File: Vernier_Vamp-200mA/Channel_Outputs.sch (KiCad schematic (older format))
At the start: 63 parts, among them U12 OPA2277, U13 OPA2277, U14 OPA2277, U15 OPA1622, U16 OPA1622, U17 OPA1622

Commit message: Coil driver version 1.0B
Updated coil driver 200mA version with fixes requested by Iain.
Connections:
- net labels added: +7.5V, -7.5V
- net labels removed: +8V, -8V
- wire segments 240 -> 239
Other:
- note added: "OP-AMP decoupling"
- moved on the sheet: C1, C2, C3, C31, C32, C33, C37, C38, C39, C40, C41, C42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

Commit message: OPA1622 Power Pad Tented Vias
-Created a footprint for OPA1622 that features tented vias on the power pad

-Applied it to the schematic as well as layout
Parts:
- U15, U16, U17: footprint Package_SON:Texas_S-PVSON-N10_ThermalVias -> PVSON-10_ThermalVias-Tented:Texas_S-PVSON-10_ThermalVias-Tented
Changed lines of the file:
@@
 $Descr A4 11693 8268
 encoding utf-8
-Sheet 7 7
+Sheet 6 7
 Title "\"Vernier Vamp\" Coil Driver - 200mA"
 Date "2020-04-27"
@@
 F 0 "U15" H 4350 1650 50  0000 C CNN
 F 1 "OPA1622" H 4350 1550 50  0000 C CNN
-F 2 "Package_SON:Texas_S-PVSON-N10_ThermalVias" H 4150 1000 50  0001 C CNN
+F 2 "PVSON-10_ThermalVias-Tented:Texas_S-PVSON-10_ThermalVias-Tented" H 4150 1000 50  0001 C CNN
 F 3 "http://www.ti.com/lit/ds/symlink/opa1622.pdf" H 4150 1400 50  0001 C CNN
 	1    4150 1400
@@
 F 0 "U15" H 4300 2750 50  0000 C CNN
 F 1 "OPA1622" H 4300 2650 50  0000 C CNN
-F 2 "Package_SON:Texas_S-PVSON-N10_ThermalVias" H 4150 2100 50  0001 C CNN
+F 2 "PVSON-10_ThermalVias-Tented:Texas_S-PVSON-10_ThermalVias-Tented" H 4150 2100 50  0001 C CNN
 F 3 "http://www.ti.com/lit/ds/symlink/opa1622.pdf" H 4150 2500 50  0001 C CNN
 	2    4150 2500
@@
 F 0 "U15" H 4194 1400 50  0001 L CNN
 F 1 "OPA1622" H 4194 1355 50  0001 L CNN
-F 2 "Package_SON:Texas_S-PVSON-N10_ThermalVias" H 4150 1000 50  0001 C CNN
+F 2 "PVSON-10_ThermalVias-Tented:Texas_S-PVSON-10_ThermalVias-Tented" H 4150 1000 50  0001 C CNN
 F 3 "http://www.ti.com/lit/ds/symlink/opa1622.pdf" H 4150 1400 50  0001 C CNN
 	3    4150 1400
@@
 F 0 "U16" H 4350 4350 50  0000 C CNN
 F 1 "OPA1622" H 4350 4250 50  0000 C CNN
-F 2 "Package_SON:Texas_S-PVSON-N10_ThermalVias" H 4150 3700 50  0001 C CNN
+F 2 "PVSON-10_ThermalVias-Tented:Texas_S-PVSON-10_ThermalVias-Tented" H 4150 3700 50  0001 C CNN
 F 3 "http://www.ti.com/lit/ds/symlink/opa1622.pdf" H 4150 4100 50  0001 C CNN
 	1    4150 4100
@@
 F 0 "U16" H 4300 5450 50  0000 C CNN
 F 1 "OPA1622" H 4300 5350 50  0000 C CNN
-F 2 "Package_SON:Texas_S-PVSON-N10_ThermalVias" H 4150 4800 50  0001 C CNN
+F 2 "PVSON-10_ThermalVias-Tented:Texas_S-PVSON-10_ThermalVias-Tented" H 4150 4800 50  0001 C CNN
 F 3 "http://www.ti.com/lit/ds/symlink/opa1622.pdf" H 4150 5200 50  0001 C CNN
 	2    4150 5200
@@
 F 0 "U16" H 4194 4100 50  0001 L CNN
 F 1 "OPA1622" H 4194 4055 50  0001 L CNN
-F 2 "Package_SON:Texas_S-PVSON-N10_ThermalVias" H 4150 3700 50  0001 C CNN
+F 2 "PVSON-10_ThermalVias-Tented:Texas_S-PVSON-10_ThermalVias-Tented" H 4150 3700 50  0001 C CNN
 F 3 "http://www.ti.com/lit/ds/symlink/opa1622.pdf" H 4150 4100 50  0001 C CNN
 	3    4150 4100
@@
 F 0 "U17" H 9550 1650 50  0000 C CNN
 F 1 "OPA1622" H 9550 1550 50  0000 C CNN
-F 2 "Package_SON:Texas_S-PVSON-N10_ThermalVias" H 9350 1000 50  0001 C CNN
+F 2 "PVSON-10_ThermalVias-Tented:Texas_S-PVSON-10_ThermalVias-Tented" H 9350 1000 50  0001 C CNN
 F 3 "http://www.ti.com/lit/ds/symlink/opa1622.pdf" H 9350 1400 50  0001 C CNN
 	1    9350 1400
@@
 F 0 "U17" H 9500 2750 50  0000 C CNN
 F 1 "OPA1622" H 9500 2650 50  0000 C CNN
-F 2 "Package_SON:Texas_S-PVSON-N10_ThermalVias" H 9350 2100 50  0001 C CNN
+F 2 "PVSON-10_ThermalVias-Tented:Texas_S-PVSON-10_ThermalVias-Tented" H 9350 2100 50  0001 C CNN
 F 3 "http://www.ti.com/lit/ds/symlink/opa1622.pdf" H 9350 2500 50  0001 C CNN
 	2    9350 2500
@@
 F 0 "U17" H 9394 1400 50  0001 L CNN
 F 1 "OPA1622" H 9394 1355 50  0001 L CNN
-F 2 "Package_SON:Texas_S-PVSON-N10_ThermalVias" H 9350 1000 50  0001 C CNN
+F 2 "PVSON-10_ThermalVias-Tented:Texas_S-PVSON-10_ThermalVias-Tented" H 9350 1000 50  0001 C CNN
 F 3 "http://www.ti.com/lit/ds/symlink/opa1622.pdf" H 9350 1400 50  0001 C CNN
 	3    9350 1400

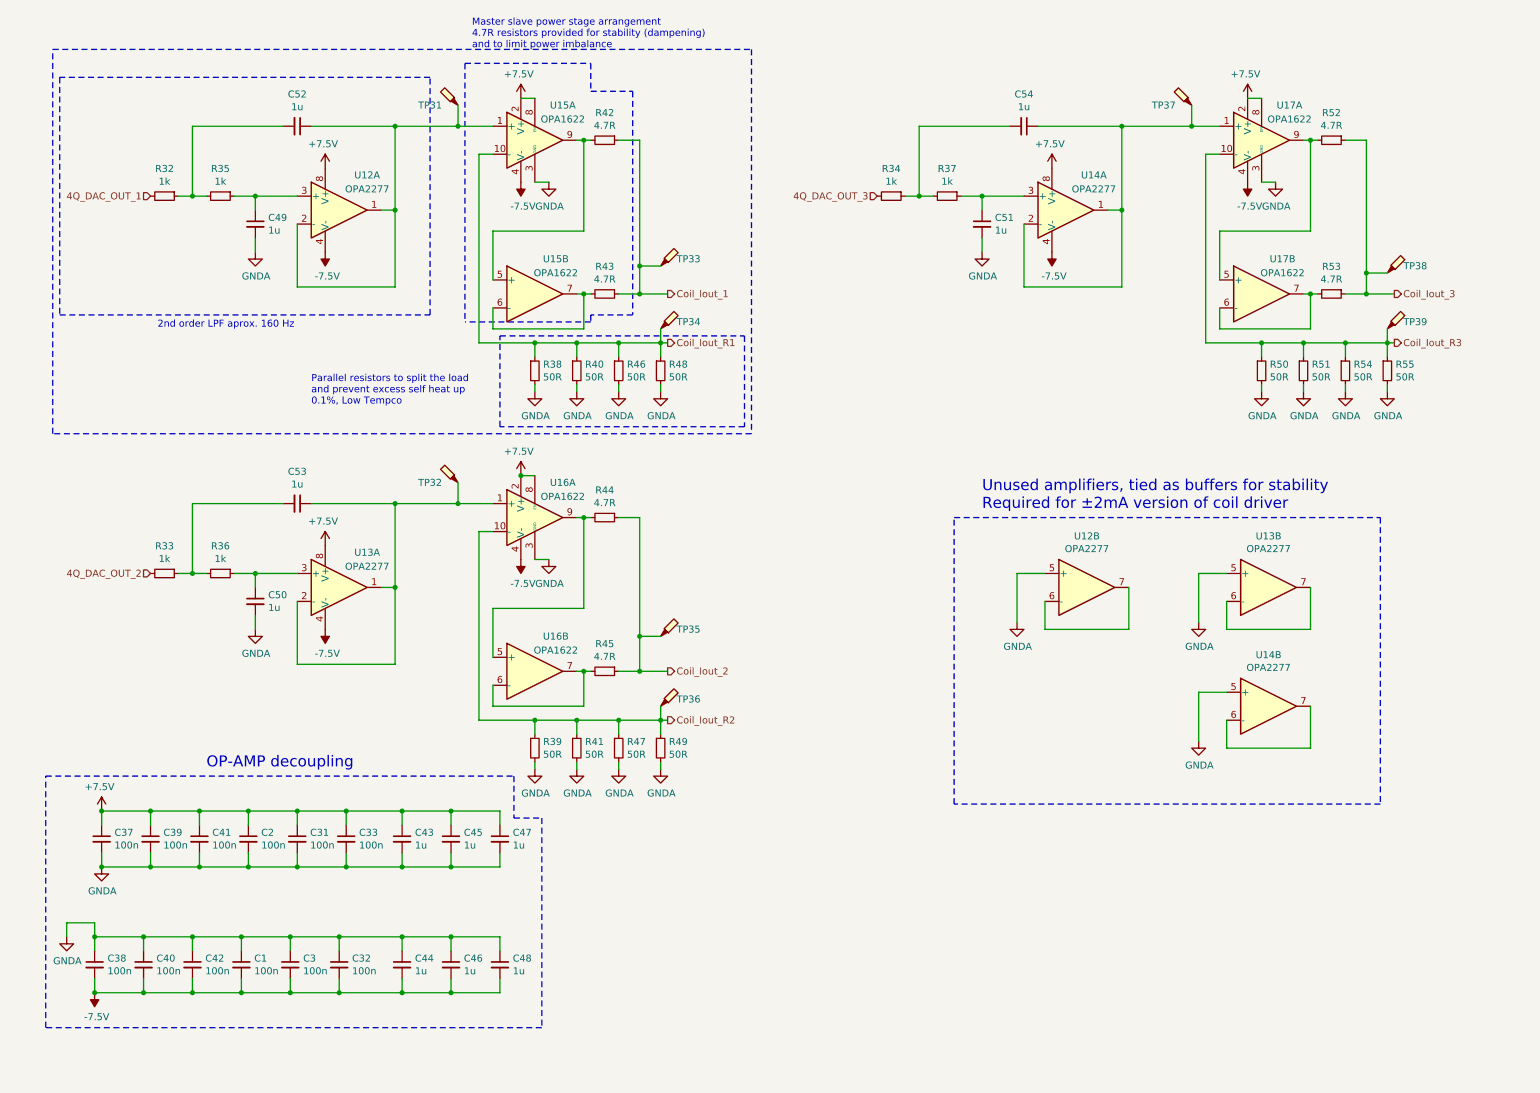
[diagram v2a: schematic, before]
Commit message: 1.0D Update
LCCD changes
-Addition of trigger for calibration
-PCB optimisation

HCCD changes
-New output stage designed
-Changes from 1.0C applied to HCCD
-New more optimised layout
-New shielding over analog section
-Addition of trigger for calibration

New symbols and footprint creation
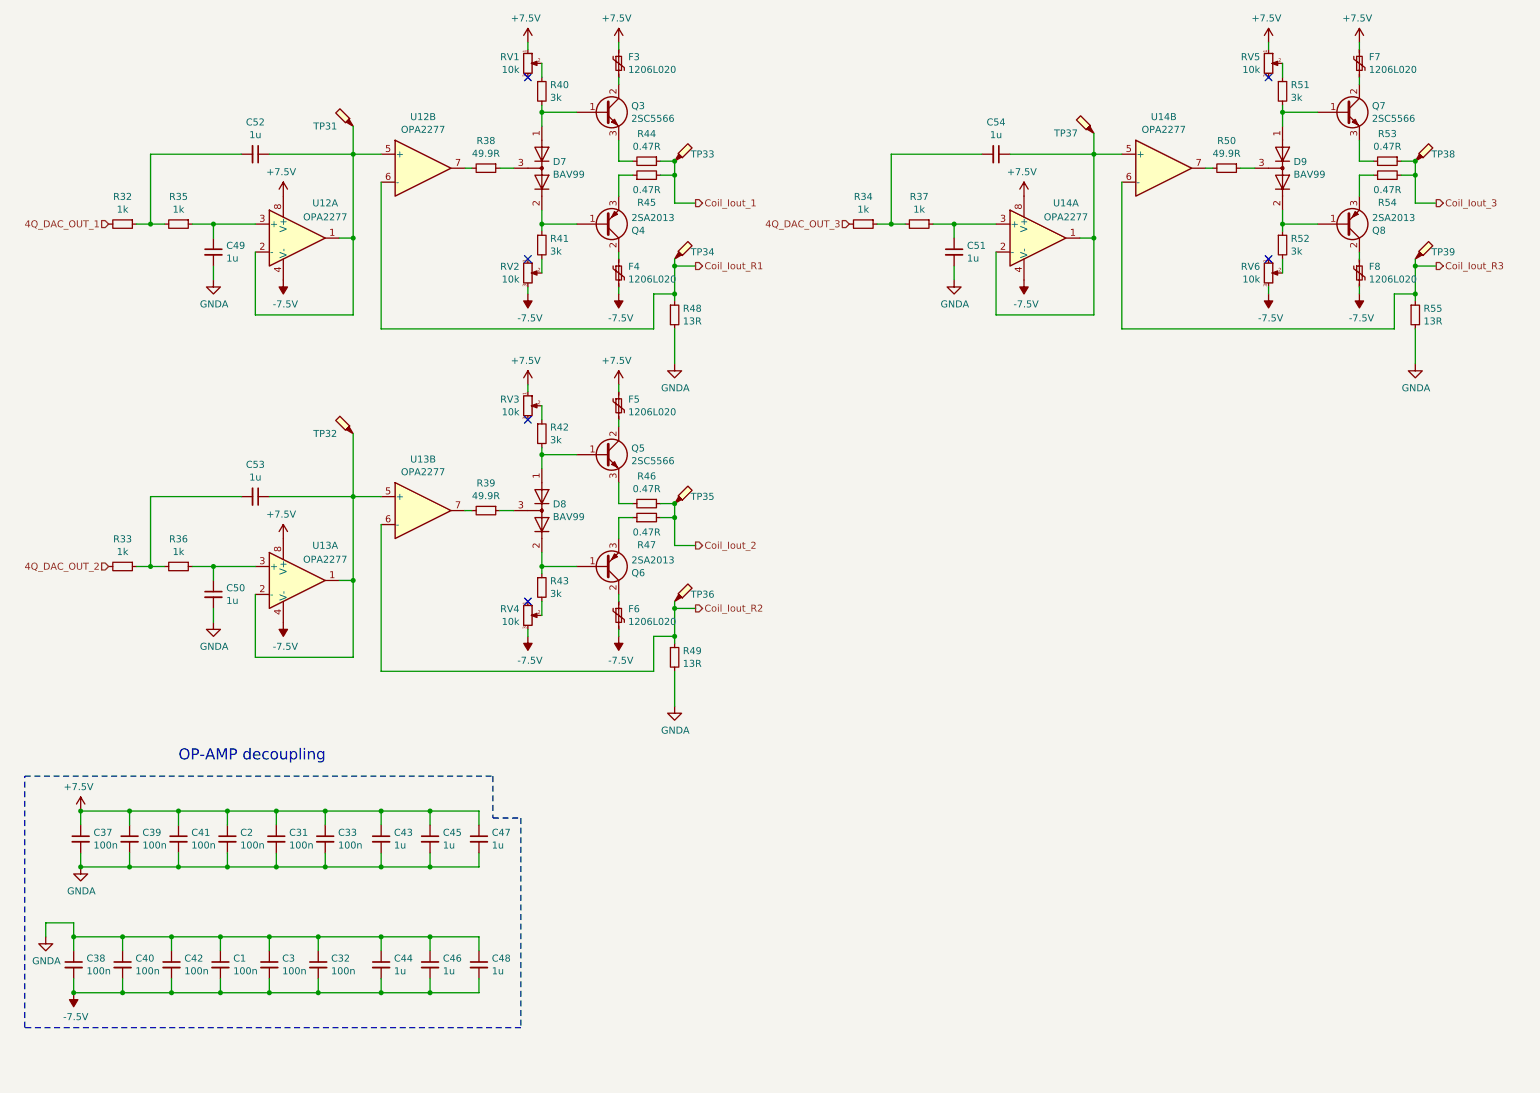
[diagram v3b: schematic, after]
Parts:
- removed U15, U16, U17: OPA1622, PVSON-10_ThermalVias-Tented:Texas_S-PVSON-10_ThermalVias-Tented, symbol Amplifier_Audio:OPA1622
- added D7, D8, D9: BAV99, Package_TO_SOT_SMD:SOT-23, symbol Diode:BAV99
- added F3, F4, F5, F6, F7, F8: 1206L020, Fuse:Fuse_1206_3216Metric, symbol Device:Polyfuse_Small
- added Q3, Q5, Q7: 2SC5566, Package_TO_SOT_SMD:SOT-89-3_Handsoldering, symbol 2SA2013_2SC5566:2SC5566
- added Q4, Q6, Q8: 2SA2013, Package_TO_SOT_SMD:SOT-89-3_Handsoldering, symbol 2SA2013_2SC5566:2SA2013
- added RV1, RV2, RV3, RV4, RV5, RV6: 10k, Potentiometer_SMD:Potentiometer_Bourns_3224W_Vertical, symbol Device:R_POT_Small
- R38, R39, R50: value 50R -> 49.9R; footprint Resistor_SMD:R_1206_3216Metric_Pad1.42x1.75mm_HandSolder -> Resistor_SMD:R_0603_1608Metric_Pad1.05x0.95mm_HandSolder
- R40, R41, R51: value 50R -> 3k; footprint Resistor_SMD:R_1206_3216Metric_Pad1.42x1.75mm_HandSolder -> Resistor_SMD:R_0603_1608Metric_Pad1.05x0.95mm_HandSolder
- R42, R43, R52: value 4.7R -> 3k; footprint Resistor_SMD:R_0805_2012Metric_Pad1.15x1.40mm_HandSolder -> Resistor_SMD:R_0603_1608Metric_Pad1.05x0.95mm_HandSolder
- R44, R45: value 4.7R -> 0.47R; footprint Resistor_SMD:R_0805_2012Metric_Pad1.15x1.40mm_HandSolder -> Resistor_SMD:R_1206_3216Metric
- R46, R47: value 50R -> 0.47R; footprint Resistor_SMD:R_1206_3216Metric_Pad1.42x1.75mm_HandSolder -> Resistor_SMD:R_1206_3216Metric
- R48, R49, R55: value 50R -> 13R; footprint Resistor_SMD:R_1206_3216Metric_Pad1.42x1.75mm_HandSolder -> WSM2-13R0-FTR-LF:WSM2 13R0 FTR-LF
- R53: value 4.7R -> 0.47R; footprint Resistor_SMD:R_0805_2012Metric_Pad1.15x1.40mm_HandSolder -> Resistor_SMD:R_1206_3216Metric_Pad1.30x1.75mm_HandSolder
- R54: value 50R -> 0.47R; footprint Resistor_SMD:R_1206_3216Metric_Pad1.42x1.75mm_HandSolder -> Resistor_SMD:R_1206_3216Metric_Pad1.30x1.75mm_HandSolder
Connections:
- net +7V5: now also F3.1, F5.1, F7.1, RV1.1, RV3.1, RV5.1
- net -7V5: now also F4.2, F6.2, F8.2, RV2.3, RV4.3, RV6.3
- net Coil_Iout_1: now also R44.1, R45.2; no longer R42.1, R43.1
- net Coil_Iout_2: now also R46.1, R47.2; no longer R44.1, R45.1
- net Coil_Iout_3: now also R54.2; no longer R52.1
- net Coil_Iout_R1: now also U12.6 (-); no longer R38.1, R40.1, R46.1
- net Coil_Iout_R2: now also U13.6 (-); no longer R39.1, R41.1, R47.1
- net Coil_Iout_R3: now also U14.6 (-); no longer R50.1, R51.1, R54.1
- net GNDA: no longer R38.2, R39.2, R40.2, R41.2, R46.2, R47.2, R50.2, R51.2, R54.2, U12.5 (+), U13.5 (+), U14.5 (+)
- net at C52.1, TP31.1, U12.1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: now also U12.5 (+)
- net at C53.1, TP32.1, U13.1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: now also U13.5 (+)
- net at C54.1, TP37.1, U14.1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: now also U14.5 (+)
- net at R42.2: now also D8.1 (K), Q5.1
- net at R43.2: now also RV4.2
- net at R44.2: now also Q3.3
- net at R52.2: now also RV6.2
- net at R53.2: now also Q7.3
- net at U12.7: now also R38.2; no longer U12.6 (-)
- net at U13.7: now also R39.2; no longer U13.6 (-)
- net at U14.7: now also R50.2; no longer U14.6 (-)
- new net: D8.2 (A), Q6.1, R43.1
- new net: F6.1, Q6.2
- new net: Q6.3, R47.1
- new net: F5.2, Q5.2
- new net: Q5.3, R46.2
- new net: R42.1, RV3.2
- new net: D8.3 (K), R39.1
- new net: D7.2 (A), Q4.1, R41.1
- new net: F4.1, Q4.2
- new net: Q4.3, R45.1
- new net: D7.1 (K), Q3.1, R40.2
- new net: F3.2, Q3.2
- new net: R41.2, RV2.2
- new net: D7.3 (K), R38.1
- new net: R40.1, RV1.2
- new net: D9.2 (A), Q8.1, R52.1
- new net: F8.1, Q8.2
- new net: Q8.3, R54.1
- new net: D9.1 (K), Q7.1, R51.2
- new net: F7.2, Q7.2
- new net: D9.3 (K), R50.1
- new net: R51.1, RV5.2
- no-connect marks 0 -> 6
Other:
- note removed: "2nd order LPF aprox. 160 Hz"
- note removed: "Master slave power stage arrangement\n4.7R resistors provided for stability (dampening)\nand to limit power imbalance\n"
- note removed: "Parallel resistors to split the load\nand prevent excess self heat up\n0.1%, Low Tempco"
- note removed: "Unused amplifiers, tied as buffers for stability\nRequired for ±2mA version of coil driver"
- moved on the sheet: C1, C2, C3, C31, C32, C33, C37, C38, C39, C40, C41, C42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

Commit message: Update Channel_Outputs.sch
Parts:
- added TP49, TP50, TP51, TP52, TP53, TP54: TestPoint_Probe, TestPoint:TestPoint_Pad_D1.0mm, symbol Connector:TestPoint_Probe
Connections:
- net Coil_Iout_R1: now also TP49.1
- net Coil_Iout_R2: now also TP51.1
- net Coil_Iout_R3: now also TP53.1
- net GNDA: now also TP50.1, TP52.1, TP54.1
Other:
- note added: "SMA test outputs\n"
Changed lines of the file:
@@
 Wire Wire Line
 	8350 1500 8150 1500
+Text Notes 7850 4250 0    50   ~ 0
+SMA test outputs\n
+Text HLabel 7550 4400 0    50   Output ~ 0
+Coil_Iout_R1
+Text HLabel 7550 5000 0    50   Output ~ 0
+Coil_Iout_R2
+Text HLabel 7550 5650 0    50   Output ~ 0
+Coil_Iout_R3
+$Comp
+L power:GNDA #PWR019
+U 1 1 60AC48A3
+P 8200 4600
+F 0 "#PWR019" H 8200 4350 50  0001 C CNN
+F 1 "GNDA" H 8205 4427 50  0000 C CNN
+F 2 "" H 8200 4600 50  0001 C CNN
+F 3 "" H 8200 4600 50  0001 C CNN
+	1    8200 4600
+	1    0    0    -1
+$EndComp
+$Comp
+L power:GNDA #PWR020
+U 1 1 60AE753F
+P 8200 5200
+F 0 "#PWR020" H 8200 4950 50  0001 C CNN
+F 1 "GNDA" H 8205 5027 50  0000 C CNN
+F 2 "" H 8200 5200 50  0001 C CNN
+F 3 "" H 8200 5200 50  0001 C CNN
+	1    8200 5200
+	1    0    0    -1
+$EndComp
+$Comp
+L power:GNDA #PWR021
+U 1 1 60AFE47F
+P 8200 5850
+F 0 "#PWR021" H 8200 5600 50  0001 C CNN
+F 1 "GNDA" H 8205 5677 50  0000 C CNN
+F 2 "" H 8200 5850 50  0001 C CNN
+F 3 "" H 8200 5850 50  0001 C CNN
+	1    8200 5850
+	1    0    0    -1
+$EndComp
+$Comp
+L Connector:TestPoint_Probe TP?
+U 1 1 60B23305
+P 8200 4400
+AR Path="/5E1DEB8C/60B23305" Ref="TP?"  Part="1"
+AR Path="/5E1E279E/60B23305" Ref="TP49"  Part="1"
+F 0 "TP49" H 8400 4450 50  0000 C CNN
+F 1 "TestPoint_Probe" V 8399 4455 50  0001 C CNN
+F 2 "TestPoint:TestPoint_Pad_D1.0mm" H 8400 4400 50  0001 C CNN
+F 3 "~" H 8400 4400 50  0001 C CNN
+	1    8200 4400
+	1    0    0    -1
+$EndComp
+$Comp
+L Connector:TestPoint_Probe TP?
+U 1 1 60B3A087
+P 8200 4600
+AR Path="/5E1DEB8C/60B3A087" Ref="TP?"  Part="1"
+AR Path="/5E1E279E/60B3A087" Ref="TP50"  Part="1"
+F 0 "TP50" H 8400 4650 50  0000 C CNN
+F 1 "TestPoint_Probe" V 8399 4655 50  0001 C CNN
+F 2 "TestPoint:TestPoint_Pad_D1.0mm" H 8400 4600 50  0001 C CNN
+F 3 "~" H 8400 4600 50  0001 C CNN
+	1    8200 4600
+	1    0    0    -1
+$EndComp
+Wire Wire Line
+	7550 4400 8200 4400
+$Comp
+L Connector:TestPoint_Probe TP?
+U 1 1 60B519D4
+P 8200 5000
+AR Path="/5E1DEB8C/60B519D4" Ref="TP?"  Part="1"
+AR Path="/5E1E279E/60B519D4" Ref="TP51"  Part="1"
+F 0 "TP51" H 8400 5050 50  0000 C CNN
+F 1 "TestPoint_Probe" V 8399 5055 50  0001 C CNN
+F 2 "TestPoint:TestPoint_Pad_D1.0mm" H 8400 5000 50  0001 C CNN
+F 3 "~" H 8400 5000 50  0001 C CNN
+	1    8200 5000
+	1    0    0    -1
+$EndComp
+$Comp
+L Connector:TestPoint_Probe TP?
+U 1 1 60B5D050
+P 8200 5200
+AR Path="/5E1DEB8C/60B5D050" Ref="TP?"  Part="1"
+AR Path="/5E1E279E/60B5D050" Ref="TP52"  Part="1"
+F 0 "TP52" H 8400 5250 50  0000 C CNN
+F 1 "TestPoint_Probe" V 8399 5255 50  0001 C CNN
+F 2 "TestPoint:TestPoint_Pad_D1.0mm" H 8400 5200 50  0001 C CNN
+F 3 "~" H 8400 5200 50  0001 C CNN
+	1    8200 5200
+	1    0    0    -1
+$EndComp
+Wire Wire Line
+	7550 5000 8200 5000
+$Comp
+L Connector:TestPoint_Probe TP?
+U 1 1 60B74BE6
+P 8200 5650
+AR Path="/5E1DEB8C/60B74BE6" Ref="TP?"  Part="1"
+AR Path="/5E1E279E/60B74BE6" Ref="TP53"  Part="1"
+F 0 "TP53" H 8400 5700 50  0000 C CNN
+F 1 "TestPoint_Probe" V 8399 5705 50  0001 C CNN
+F 2 "TestPoint:TestPoint_Pad_D1.0mm" H 8400 5650 50  0001 C CNN
+F 3 "~" H 8400 5650 50  0001 C CNN
+	1    8200 5650
+	1    0    0    -1
+$EndComp
+$Comp
+L Connector:TestPoint_Probe TP?
+U 1 1 60B74BEC
+P 8200 5850
+AR Path="/5E1DEB8C/60B74BEC" Ref="TP?"  Part="1"
+AR Path="/5E1E279E/60B74BEC" Ref="TP54"  Part="1"
+F 0 "TP54" H 8400 5900 50  0000 C CNN
+F 1 "TestPoint_Probe" V 8399 5905 50  0001 C CNN
+F 2 "TestPoint:TestPoint_Pad_D1.0mm" H 8400 5850 50  0001 C CNN
+F 3 "~" H 8400 5850 50  0001 C CNN
+	1    8200 5850
+	1    0    0    -1
+$EndComp
+Wire Wire Line
+	7550 5650 8200 5650
 $EndSCHEMATC
